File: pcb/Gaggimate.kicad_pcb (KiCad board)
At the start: 2 copper layers, 85 x 67 mm, 85 parts, among them J1 USB_C_Receptacle, J10 Conn_01x02, J2 Conn_01x02, J3 Conn_01x03, J4 Conn_01x04, J5 Conn_01x04, J6 Conn_01x10, J7 Conn_01x02, J8 Conn_01x02, J9 Conn_01x04, K1 Relay_SPDT, K2 Relay_SPDT, K3 Relay_SPDT, Q1 MMBT2222, Q2 MMBT2222, Q3 MMBT2222, SW1 SW_Push, SW2 SW_Push, U1 ESP32-S3-WROOM-1, U2 AMS1117-3.3, U6 MAX31855EASA

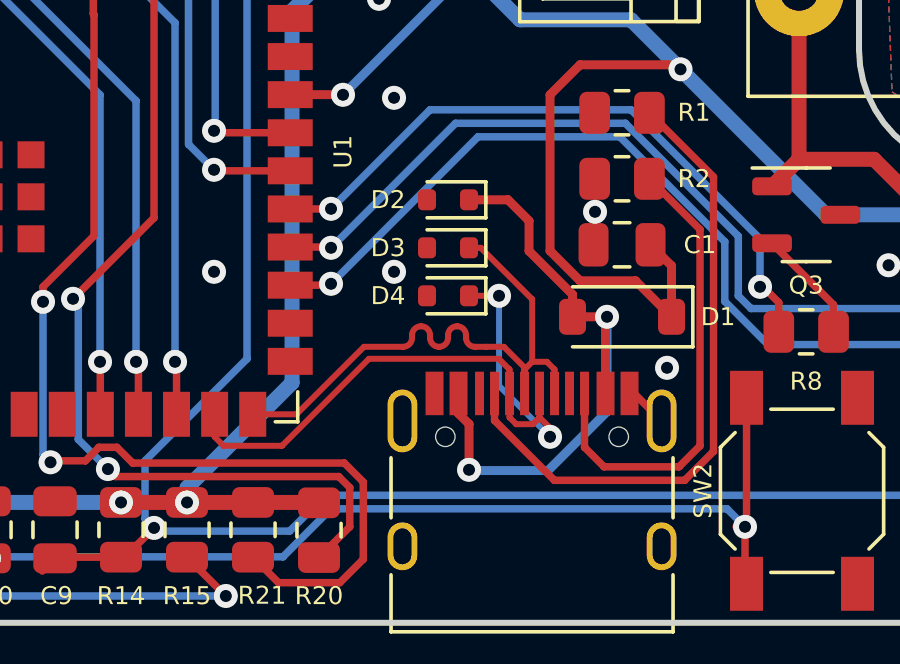
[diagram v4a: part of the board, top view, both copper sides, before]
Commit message: feat: Replace diodes with usb protection chip
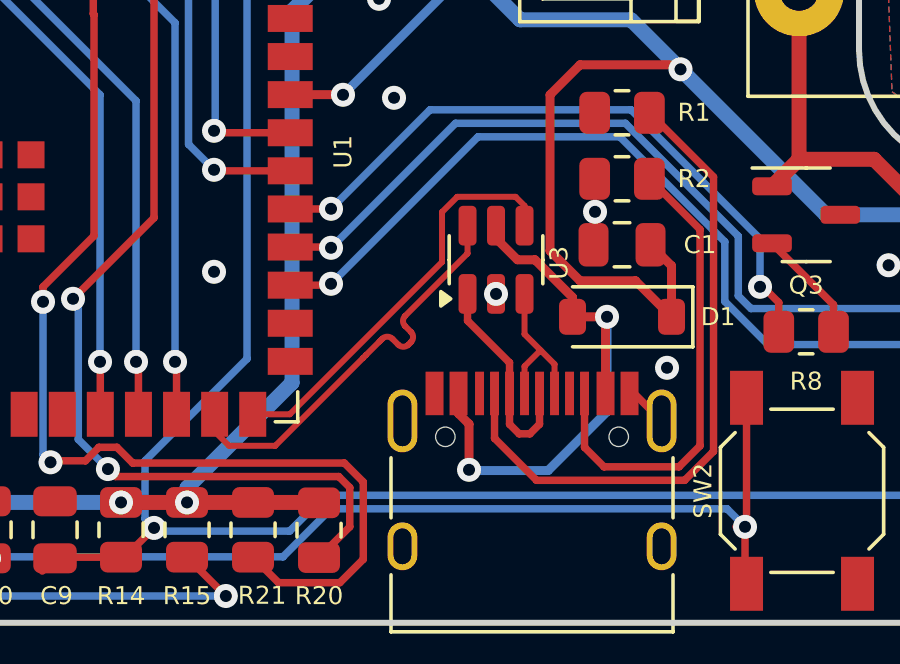
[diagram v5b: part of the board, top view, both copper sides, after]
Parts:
- removed D2, D3, D4: LESD5s, Diode_SMD:D_SOD-523
- added U3: USBLC6-2SC6, Package_TO_SOT_SMD:SOT-23-6, F.Cu at (189.2, 81.0)
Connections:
- net /VBUS renamed Net-(D1-A)
- J1 pad A6: /USB_DP -> /USB_UF_DP
- J1 pad A7: /USB_DN -> /USB_UF_DN
- J1 pad B6: /USB_DP -> /USB_UF_DP
- J1 pad B7: /USB_DN -> /USB_UF_DN
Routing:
- net /USB_DN: track 22.9 -> 13.8 mm, vias 2 -> 0
- net /USB_DP: track 21.1 -> 13.8 mm
- net /USB_UF_DN: track 0.00 -> 7.21 mm
- net /USB_UF_DP: track 0.00 -> 6.00 mm
- net Net-(D1-A): track 21.1 -> 19.5 mm

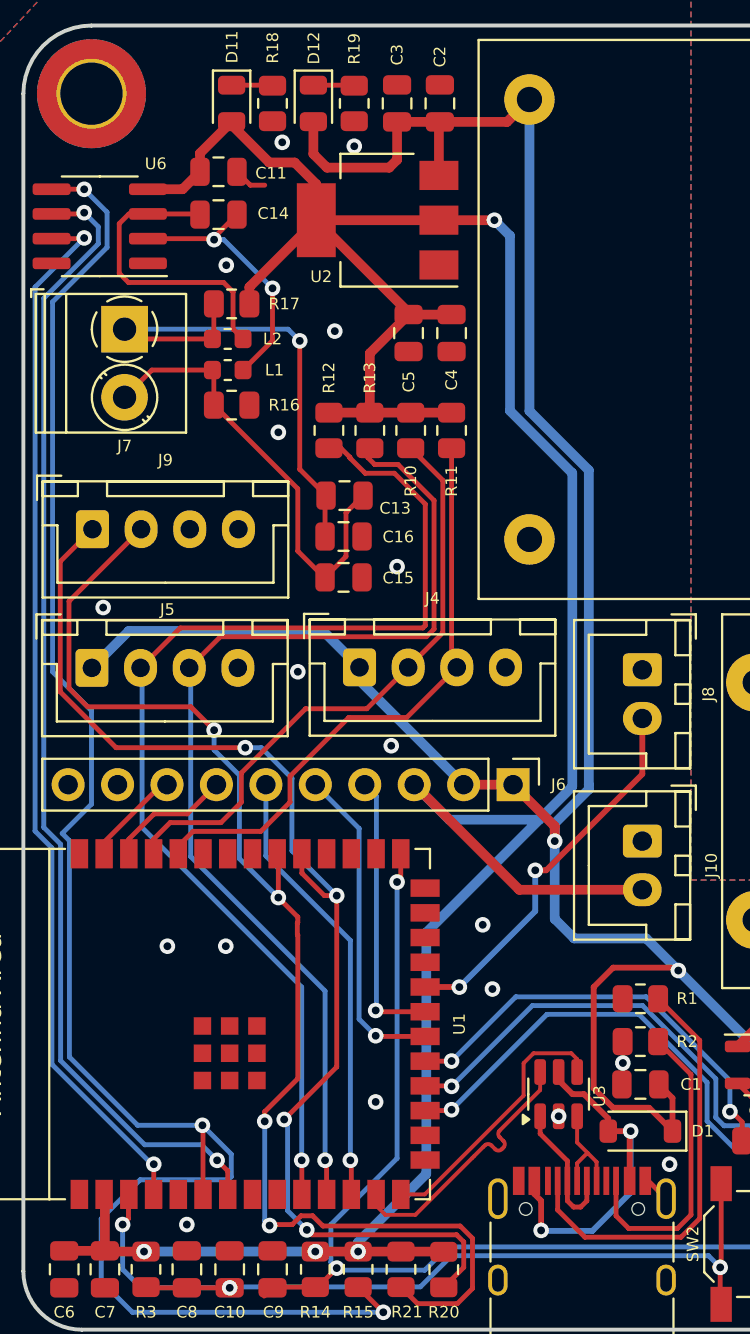
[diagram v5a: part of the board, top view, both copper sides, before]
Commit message: feat: Simplify MAX31885 circuit, add silkscreen pinout
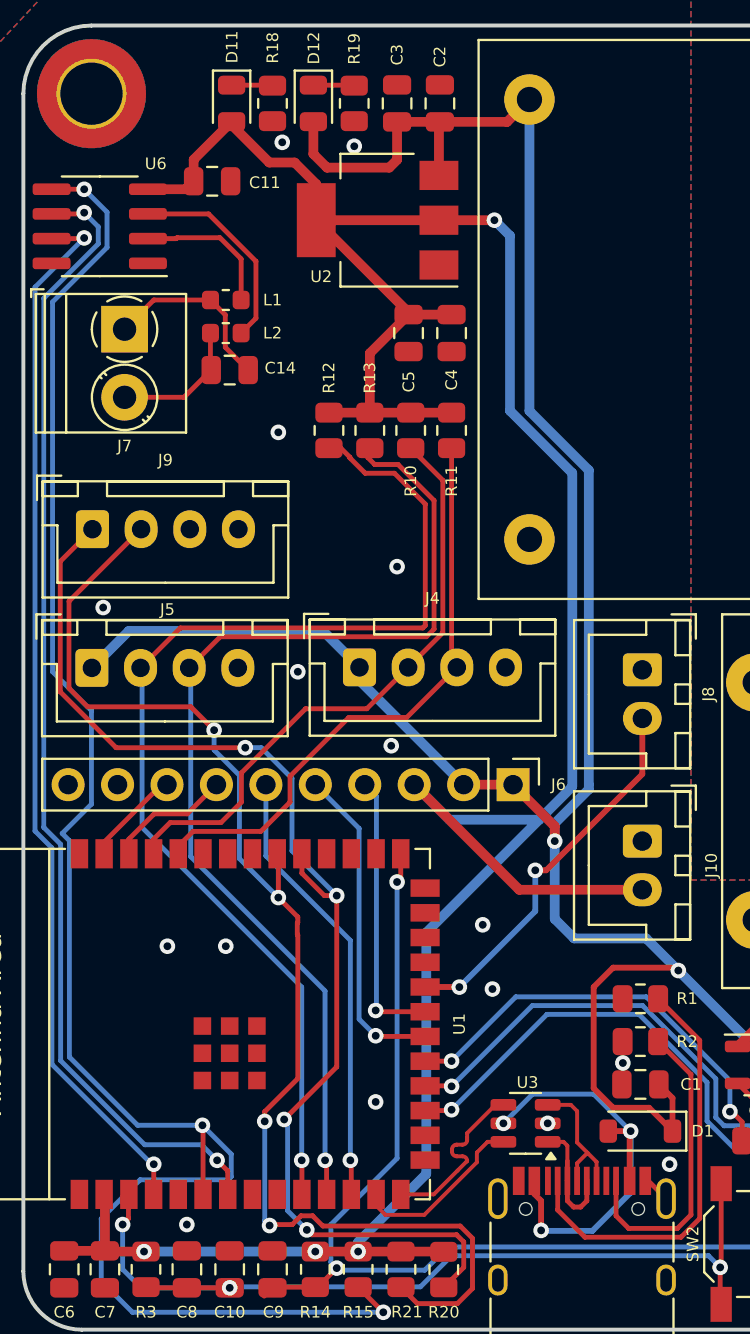
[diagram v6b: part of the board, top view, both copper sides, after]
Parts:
- removed C13: 1uF, Capacitor_SMD:C_0805_2012Metric
- removed C15, C16: 100nF, Capacitor_SMD:C_0805_2012Metric
- removed R16, R17: 1M, Resistor_SMD:R_0805_2012Metric
- removed kibuzzard-671E8BF3: G***, kibuzzard-671E8BF3
- removed kibuzzard-671E8C00: G***, kibuzzard-671E8C00
- removed kibuzzard-671E8C14: G***, kibuzzard-671E8C14
- removed kibuzzard-671E8C44: G***, kibuzzard-671E8C44
- removed kibuzzard-671E8C4D: G***, kibuzzard-671E8C4D
- removed kibuzzard-671E8D02 (x4): G***, kibuzzard-671E8D02
- removed kibuzzard-671EE717: G***, kibuzzard-671EE717
- removed kibuzzard-671EE722: G***, kibuzzard-671EE722
- added kibuzzard-67322575: G***, kibuzzard-67322575, B.Cu at (172.0, 41.8)
- added kibuzzard-6732257B: G***, kibuzzard-6732257B, B.Cu at (171.9, 45.2)
- added kibuzzard-6732261A: G***, kibuzzard-6732261A, B.Cu at (170.2, 61.5)
- added kibuzzard-67322649: G***, kibuzzard-67322649, B.Cu at (166.5, 67.3)
- added kibuzzard-67322649: G***, kibuzzard-67322649, B.Cu at (172.8, 54.2)
- added kibuzzard-67322649: G***, kibuzzard-67322649, B.Cu at (164.0, 67.3)
- added kibuzzard-67322649: G***, kibuzzard-67322649, B.Cu at (190.9, 59.2)
- added kibuzzard-67322649: G***, kibuzzard-67322649, B.Cu at (186.5, 61.5)
- added kibuzzard-67322649: G***, kibuzzard-67322649, B.Cu at (190.9, 68.0)
- added kibuzzard-67322649: G***, kibuzzard-67322649, B.Cu at (172.7, 61.5)
- added kibuzzard-67322649: G***, kibuzzard-67322649, B.Cu at (170.3, 54.2)
- added kibuzzard-67322650: G***, kibuzzard-67322650, B.Cu at (186.9, 67.4)
- added kibuzzard-67322650: G***, kibuzzard-67322650, B.Cu at (165.2, 61.5)
- added kibuzzard-67322650: G***, kibuzzard-67322650, B.Cu at (184.3, 67.4)
- added kibuzzard-67322650: G***, kibuzzard-67322650, B.Cu at (179.0, 61.5)
- added kibuzzard-67322655: G***, kibuzzard-67322655, B.Cu at (167.7, 61.5)
- added kibuzzard-6732266F: G***, kibuzzard-6732266F, B.Cu at (169.1, 67.7)
- added kibuzzard-67322681: G***, kibuzzard-67322681, B.Cu at (171.6, 67.7)
- added kibuzzard-67322686: G***, kibuzzard-67322686, B.Cu at (174.2, 67.7)
- added kibuzzard-673226A0: G***, kibuzzard-673226A0, B.Cu at (176.7, 67.9)
- added kibuzzard-673226A8: G***, kibuzzard-673226A8, B.Cu at (179.2, 67.9)
- added kibuzzard-673226AF: G***, kibuzzard-673226AF, B.Cu at (190.5, 70.5)
- added kibuzzard-673226AF: G***, kibuzzard-673226AF, B.Cu at (181.8, 67.8)
- added kibuzzard-673226B7: G***, kibuzzard-673226B7, B.Cu at (165.2, 54.4)
- added kibuzzard-673226BE: G***, kibuzzard-673226BE, B.Cu at (167.8, 54.6)
- added kibuzzard-673226D2: G***, kibuzzard-673226D2, B.Cu at (190.9, 61.7)
- added kibuzzard-6732270D: G***, kibuzzard-6732270D, B.Cu at (181.5, 61.3)
- added kibuzzard-67322714: G***, kibuzzard-67322714, B.Cu at (184.0, 61.3)
- added kibuzzard-67322749: G***, kibuzzard-67322749, B.Cu at (193.5, 65.8)
- added kibuzzard-6732274F: G***, kibuzzard-6732274F, B.Cu at (182.8, 56.9)
- added kibuzzard-67322755: G***, kibuzzard-67322755, B.Cu at (169.0, 57.1)
- added kibuzzard-67322768: G***, kibuzzard-67322768, B.Cu at (169.0, 50.0)
- added kibuzzard-6732277B: G***, kibuzzard-6732277B, B.Cu at (175.4, 63.1)
- added kibuzzard-67322783: G***, kibuzzard-67322783, B.Cu at (176.8, 43.6)
- added kibuzzard-6732278E: G***, kibuzzard-6732278E, B.Cu at (235.5, 47.5)
- added kibuzzard-67322796: G***, kibuzzard-67322796, B.Cu at (235.5, 42.3)
- added kibuzzard-6732279D: G***, kibuzzard-6732279D, B.Cu at (235.5, 52.7)
- added kibuzzard-673227A2: G***, kibuzzard-673227A2, B.Cu at (235.4, 35.7)
- added kibuzzard-673227A8: G***, kibuzzard-673227A8, B.Cu at (235.3, 30.6)
- added kibuzzard-67322833: G***, kibuzzard-67322833, B.Cu at (193.5, 57.0)
- moved C14 8.01 mm to (172.3, 43.8)
- moved L1 3.60 mm to (172.1, 40.2)
- moved U3 2.27 mm to (187.5, 82.5), turned to 180 degrees
- moved C11 0.59 mm to (171.4, 34.1)
- moved L2 0.32 mm to (172.1, 41.9)
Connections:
- C14 pad 1: Net-(U6-T+) -> Net-(J7-Pin_2)
- C14 pad 2: Net-(U6-T-) -> Net-(J7-Pin_1)
- L1 pad 1: Net-(J7-Pin_2) -> Net-(J7-Pin_1)
- L2 pad 1: Net-(J7-Pin_1) -> Net-(J7-Pin_2)
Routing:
- net Net-(J7-Pin_1): track 26.4 -> 9.44 mm, vias 1 -> 0
- net Net-(J7-Pin_2): track 23.2 -> 7.05 mm
- net Net-(U6-T-): track 14.1 -> 7.37 mm, vias 2 -> 0
- net +3.3V: track 152.7 -> 147.1 mm
- net Net-(U6-T+): track 15.8 -> 10.6 mm
- net /USB_DP: track 13.8 -> 9.12 mm
- net /USB_DN: track 13.8 -> 9.16 mm
- net Net-(D1-A): track 19.5 -> 23.0 mm, vias 2 -> 3
- net /USB_UF_DP: track 6.00 -> 7.91 mm
- net GND: track 3.57 -> 1.74 mm, vias 20 -> 18
- net /USB_UF_DN: track 7.21 -> 6.22 mm

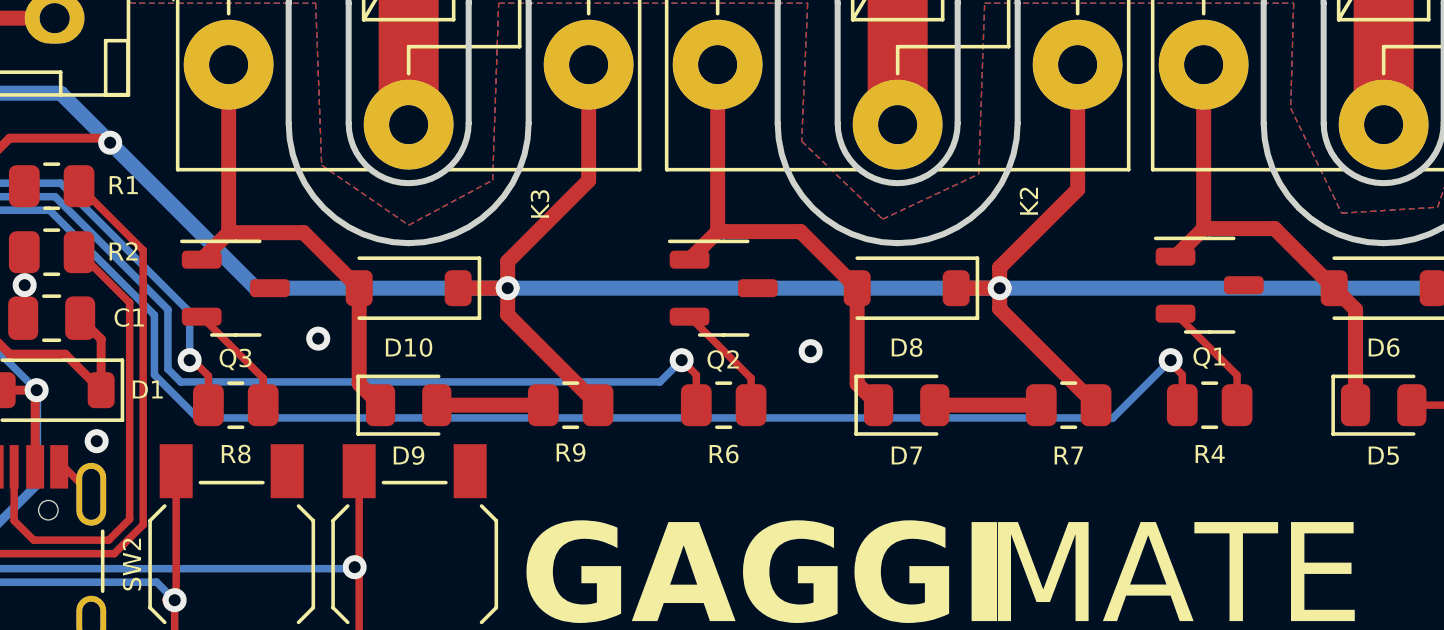
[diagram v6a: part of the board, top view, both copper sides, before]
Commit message: feat: Fix PCB label, add render
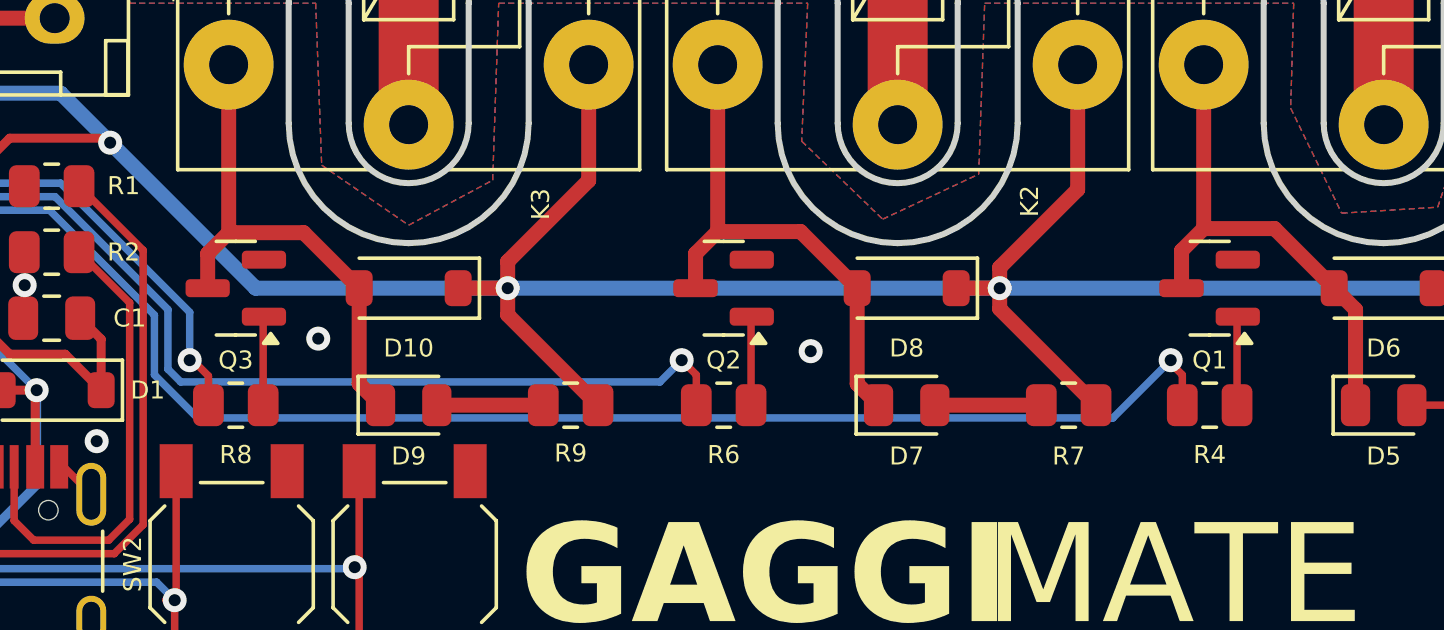
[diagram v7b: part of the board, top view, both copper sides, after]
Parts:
- removed kibuzzard-673227A2: G***, kibuzzard-673227A2
- removed kibuzzard-673227A8: G***, kibuzzard-673227A8
- added kibuzzard-6735A9F6: G***, kibuzzard-6735A9F6, B.Cu at (235.4, 35.7)
- added kibuzzard-6735A9FB: G***, kibuzzard-6735A9FB, B.Cu at (235.3, 30.6)
- Q1, Q2, Q3: value MMBT2222 -> MMBT2222A; footprint Package_TO_SOT_SMD:SOT-23-3 -> Package_TO_SOT_SMD:SOT-23
- moved Q1 0.10 mm to (232.0, 79.5), turned to 180 degrees
- turned Q2 to 180 degrees
- turned Q3 to 180 degrees
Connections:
- D6 pad 1: +5V -> unconnected-(D6-K-Pad1)
- K1 pad A1: +5V -> Net-(K1-PadA1)
- Q1 pad 1: Net-(D5-K) -> Net-(Q1-B)
- Q1 pad 2: Net-(Q1-B) -> GND
- Q1 pad 3: GND -> Net-(D5-K)
- Q2 pad 1: Net-(D7-K) -> Net-(Q2-B)
- Q2 pad 2: Net-(Q2-B) -> GND
- Q2 pad 3: GND -> Net-(D7-K)
- Q3 pad 1: Net-(D10-A) -> Net-(Q3-B)
- Q3 pad 2: Net-(Q3-B) -> GND
- Q3 pad 3: GND -> Net-(D10-A)
- R5 pad 2: +5V -> Net-(K1-PadA1)
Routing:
- net Net-(D5-K): track 16.2 -> 17.1 mm
- net Net-(D10-A): track 16.2 -> 17.1 mm
- net Net-(D7-K): track 16.5 -> 17.4 mm
- net Net-(Q2-B): track 3.80 -> 2.95 mm
- net Net-(Q3-B): track 3.80 -> 2.95 mm
- net Net-(Q1-B): track 3.90 -> 3.08 mm
